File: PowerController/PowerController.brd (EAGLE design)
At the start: 57.1 x 63.5 mm, 97 parts, among them J11 M10X2, Q1 INFINEON_2N7002_DW, Q2 INFINEON_2N7002_DW, Q3 BS250F, Q4 BS250F, Q5 INFINEON_2N7002_DW, Q6 INFINEON_2N7002_DW, Q7 INFINEON_2N7002_DW, U1 MSP430F5521/5/7/9_PN80, U2 LTV-817, U3 SN74LV74, U4 SN74LV08

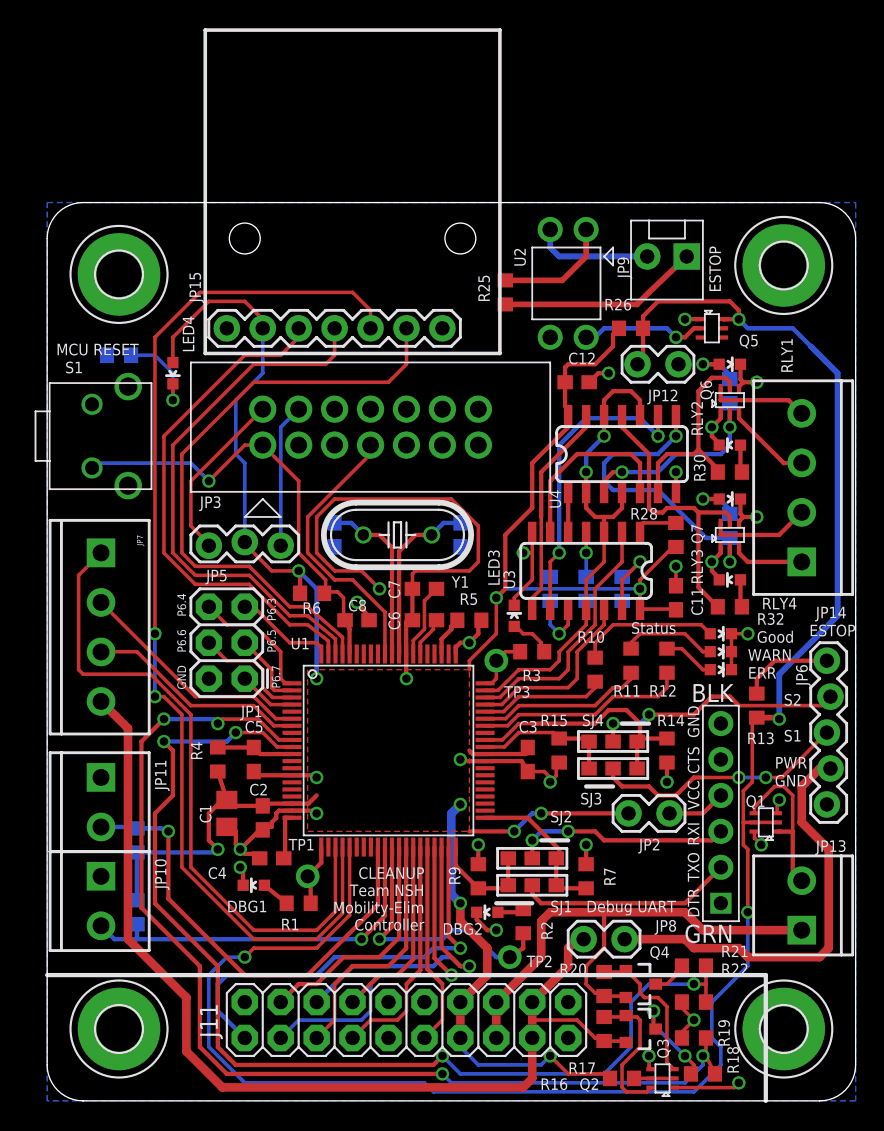
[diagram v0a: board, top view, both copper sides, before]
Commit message: Removed irrelevant circuits for PC2CAN and Power Controller
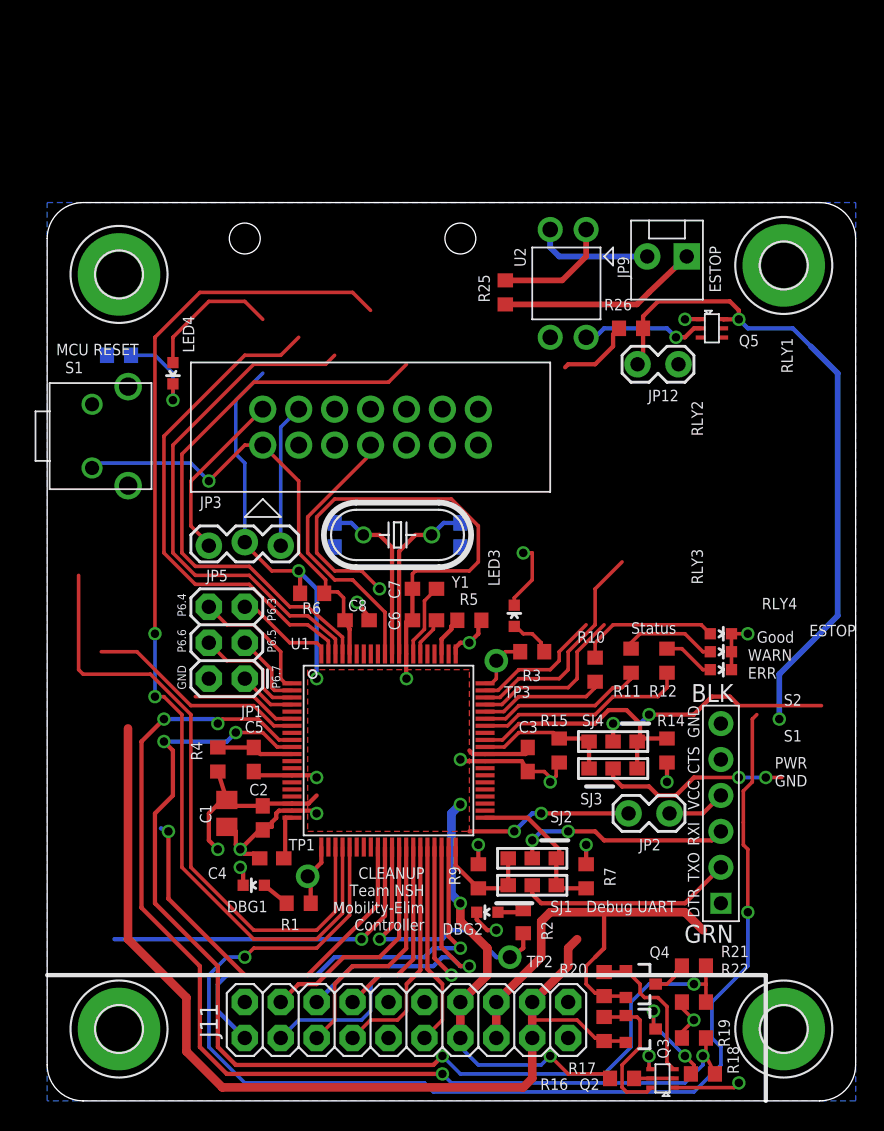
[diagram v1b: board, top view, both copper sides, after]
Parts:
- removed C11, C12: 0.1uF, rcl:C0603
- removed JP10, JP11, JP13: M023.5MM, SparkFun-Connectors:SCREWTERMINAL-3.5MM-2
- removed JP14, JP7: (no value), SparkFun-Connectors:SCREWTERMINAL-3.5MM-4
- removed JP15: (no value), SparkFun-Connectors:1X07
- removed JP6: (no value), SparkFun-Connectors:1X05_LOCK
- removed JP8: M02LOCK, SparkFun-Connectors:1X02_LOCK
- removed LED10, LED11, LED8, LED9: (no value), SparkFun-LED:LED-0603
- removed Q1, Q6, Q7: INFINEON_2N7002_DW, npol-discrete:INFINEON_SOT363
- removed R13, R27, R28, R33, R34: 0, rcl:R0603
- removed R23, R24: 10k, rcl:R0603
- removed R29, R30, R31, R32: 1k, rcl:R0603
- removed U3: SN74LV74, npol-digital:TI_D_R-PDSO-G14_SOIC14
- removed U4: SN74LV08, npol-digital:TI_D_R-PDSO-G14_SOIC14
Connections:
- removed net DRILL_RELAY_1: JP14.4, Q6.6
- removed net DRILL_RELAY_2: JP14.3, Q6.3
- removed net DRILL_RELAY_3: JP14.2, Q7.6
- removed net DRILL_RELAY_4: JP14.1, Q7.3
- removed net ESTOP_RELAY: JP13.2, Q1.1, Q1.4
- removed net N$14: LED9.A, R30.1
- removed net N$20: U3.5, U4.1
- removed net N$22: U3.6, U4.5
- removed net N$23: U3.9, U4.9
- removed net N$25: U3.8, U4.13
- removed net N$26: R27.1, U3.4
- removed net N$27: R28.2, U3.1
- removed net N$28: R33.1, U3.10
- removed net N$29: R34.2, U3.13
- removed net N$33: LED11.A, R32.1
- removed net RC_PWR: JP6.2, JP8.1
- removed net RC_S3: JP6.5, R13.2
- removed net RELAY1_CNTRL: Q6.2, R29.2, U4.3
- removed net RELAY1_LED_A: LED8.A, R29.1
- removed net RELAY2_CNTRL: Q6.5, R30.2, U4.6
- removed net RELAY3_CNTRL: Q7.2, R31.2, U4.8
- removed net RELAY3_LED_A: LED10.A, R31.1
- removed net RELAY4_CNTRL: Q7.5, R32.2, U4.11
- removed net VOC: JP15.7
- net +12V: no longer JP13.1
- net +3V3: no longer C11.1, C12.1, JP15.2, R23.2, R24.2, R27.2, R28.1, R33.2, R34.1, U3.14, U4.14
- net +5V: no longer JP7.4, JP8.2
- net DRILL_EN: no longer U3.11, U3.3, U4.10, U4.12, U4.2, U4.4
- net DRILL_ISENSE_/FAULT: no longer JP15.5
- net DRILL_ISENSE_FAULT_EN: no longer JP15.6
- net DRILL_ISENSE_VIOUT: no longer JP15.3
- net DRILL_ISENSE_VZCR: no longer JP15.4
- net DRILL_S1: no longer U3.2
- net DRILL_S2: no longer U3.12
- net ESTOP_LOCAL: no longer Q1.2, Q1.5, R13.1
- net GND: no longer C11.2, C12.2, JP10.1, JP11.1, JP15.1, JP6.1, LED10.C, LED11.C, LED8.C, LED9.C, Q1.3, Q1.6, Q6.1, Q6.4, Q7.1, Q7.4, U3.7, U4.7
- net LOWER_SWITCH: no longer JP11.2, R24.1
- net RC_S1: no longer JP6.3
- net RC_S2: no longer JP6.4
- net STEPPER_DIR: no longer JP7.2
- net STEPPER_EN: no longer JP7.3
- net STEPPER_STEP: no longer JP7.1
- net UPPER_SWITCH: no longer JP10.2, R23.1
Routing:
- net +3V3: track 162.1 -> 104.0 mm, vias 10 -> 8
- net RC_PWR: track 30.0 -> 0.00 mm
- net DRILL_EN: track 34.1 -> 9.44 mm, vias 2 -> 0
- net RELAY3_CNTRL: track 21.9 -> 0.00 mm, vias 2 -> 0
- net N$23: track 21.6 -> 0.00 mm, vias 2 -> 0
- net RELAY4_CNTRL: track 21.2 -> 0.00 mm
- net GND: track 111.5 -> 92.0 mm, vias 29 -> 20
- net N$25: track 15.2 -> 0.00 mm
- net RELAY2_CNTRL: track 14.8 -> 0.00 mm
- net RELAY1_CNTRL: track 14.8 -> 0.00 mm, vias 2 -> 0
- net N$22: track 13.1 -> 0.00 mm
- net ESTOP_RELAY: track 11.4 -> 0.00 mm
- net STEPPER_DIR: track 16.9 -> 7.48 mm
- net DRILL_RELAY_3: track 7.18 -> 0.00 mm
- net +12V: track 38.2 -> 31.2 mm
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
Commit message: Power Controller ready for fab
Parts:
- removed JP12: M02LOCK, SparkFun-Connectors:1X02_LOCK
- removed JP9: M02POLAR_LOCK, SparkFun-Connectors:MOLEX-1X2_LOCK
- removed U2: LTV-817, npol-digital:LITEON_DIL04_.3
- added JP6: (no value), SparkFun-Connectors:1X03_LOCK
- added JP7: M02POLAR_LOCK, SparkFun-Connectors:MOLEX-1X2_LOCK
- added LED10, LED8, LED9: (no value), SparkFun-LED:LED-0603
- added Q1: INFINEON_2N7002_DW, npol-discrete:INFINEON_SOT363
- added R13, R23: 10k, rcl:R0603
- added R24: 470, rcl:R0603
- added R27: 330, rcl:R0603
- added XB1: XBEE, microbuilder:XBEE
- H3: value MOUNT-PAD-ROUND3.2 -> MOUNT-HOLE3.2; device holes:3,2-PAD -> holes:3,2
- JP1: device SparkFun-Connectors:2X3 -> SparkFun-Connectors:1X05
- JP2: value M02LOCK -> (none); device SparkFun-Connectors:1X02_LOCK -> SparkFun-Connectors:2X3
- JP3: value ONSHORE_OST302-S141 -> M02LOCK; device npol-connectors:ONSHORE_OST302-S141 -> SparkFun-Connectors:1X02_LOCK
- JP4: value FTDI_DEVICE -> ONSHORE_OST302-S141; device SparkFun-Connectors:FTDI_DEVICE_SIDE -> npol-connectors:ONSHORE_OST302-S141
- JP5: value (none) -> FTDI_DEVICE; device SparkFun-Connectors:1X03_LOCK -> SparkFun-Connectors:FTDI_DEVICE_SIDE
- Q2: value INFINEON_2N7002_DW -> BS250F; device npol-discrete:INFINEON_SOT363 -> SparkFun-DiscreteSemi:SOT23-3
- Q4: value BS250F -> INFINEON_2N7002_DW; device SparkFun-DiscreteSemi:SOT23-3 -> npol-discrete:INFINEON_SOT363
- R17, R20: value 10k -> 100k
- R19, R21: value 100k -> 10k
- R25: value 620 -> 330
- R26: value 10k -> 470
- moved R22 50.4 mm to (12.7, 45.1), turned to 180 degrees
- moved JP5 44.7 mm to (55.2, 17.1), turned to 90 degrees
- moved JP4 42.6 mm to (5.08, 22.2), turned to 270 degrees
- moved Q4 42.4 mm to (24.8, 47.0), turned to 180 degrees
- moved JP1 37.2 mm to (49.5, 19.1), turned to 180 degrees
- moved JP3 31.7 mm to (33.7, 17.8)
- moved Q5 31.0 mm to (17.1, 46.4)
- moved JP2 28.9 mm to (14.0, 29.8), turned to 90 degrees
- moved R8 26.0 mm to (30.5, 47.0), flipped to the top, turned to 0 degrees
- moved R25 25.8 mm to (9.53, 45.1), turned to 90 degrees
- moved R15 23.6 mm to (40.6, 1.59), turned to 180 degrees
- moved LED4 21.7 mm to (30.5, 48.9), turned to 90 degrees
- moved R26 17.6 mm to (24.1, 50.8), turned to 270 degrees
- moved R14 12.1 mm to (35.6, 33.7), turned to 270 degrees
- moved R3 11.3 mm to (31.1, 42.5), turned to 270 degrees
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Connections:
- removed net DRILL_EN: U1.59
- removed net DRILL_ISENSE_/FAULT: U1.24
- removed net DRILL_ISENSE_FAULT_EN: U1.77
- removed net DRILL_ISENSE_VIOUT: U1.79
- removed net DRILL_ISENSE_VZCR: U1.78
- removed net DRILL_S1: U1.58
- removed net DRILL_S2: U1.57
- removed net ESTOP+: JP9.1, R25.2
- removed net ESTOP-: JP9.2, U2.2
- removed net ESTOP_LOCAL: JP12.1, Q5.6, R26.2, U1.25
- removed net ESTOP_LOCAL_INV: Q5.2, U2.4
- removed net LOWER_SWITCH: U1.29
- removed net RC_RXD: R14.2, SJ3.3, SJ4.1, U1.52
- removed net RC_S1: SJ3.2
- removed net RC_S2: SJ4.2
- removed net RC_TXD: R15.2, SJ3.1, SJ4.3, U1.51
- removed net STEPPER_DIR: U1.6
- removed net STEPPER_EN: U1.7
- removed net STEPPER_STEP: U1.23
- removed net UPPER_SWITCH: U1.30
- new net ESTOP_INV: LED8.C, Q4.5, Q4.6, R23.2, U1.22
- new net ESTOP_OUT: JP7.1, Q4.2, Q5.6, R25.2
- new net ESTOP_PULLDOWN: Q5.2, Q5.5, R22.1, U1.23
- new net N$14: LED10.C, R27.1
- new net N$15: LED8.A, R24.2
- new net N$16: Q4.3, R26.2
- new net N$17: LED9.C, R26.1
- new net NU_P3.7: JP1.5, U1.44
- new net NU_P4.0: JP1.4, U1.45
- new net NU_P4.1: JP1.3, U1.46
- new net NU_P4.2: JP1.2, U1.47
- new net NU_P4.3: JP1.1, U1.48
- new net XBEE_DIN: SJ3.2, XB1.3
- new net XBEE_DOUT: SJ4.2, XB1.2
- new net XBEE_RXD: R13.2, SJ3.3, SJ4.1, U1.52
- new net XBEE_TXD: R14.2, SJ3.1, SJ4.3, U1.51
- net +12V: now also Q3.2, R19.2, R25.1; no longer Q4.2, R20.2
- net +3V3: now also JP3.1, JP6.2, LED10.A, LED9.A, R15.2, R23.1, R24.1, XB1.1; no longer JP2.1, JP5.2, R16.2, R26.1
- net +5V: now also Q2.2, R16.2; no longer Q3.2, R17.2
- net 12VSENSE: now also R20.1, R21.2; no longer R21.1, R22.2
- net 5VSENSE: now also R17.1, R18.2; no longer R18.1, R19.2
- net GND: now also JP2.2, JP4.9, JP5.P$6, JP7.2, Q1.1, Q1.4, Q4.1, Q4.4, Q5.4, R13.1, R18.1, R21.1, R22.2, XB1.10; no longer H3.B3,2, JP1.2, JP12.2, JP3.9, JP4.P$6, Q2.1, Q2.4, R15.1, R19.1, R22.1, U2.3
- net N$1: now also JP3.2, JP5.P$4; no longer JP2.2, JP4.P$4
- net N$10: now also Q1.6, Q2.1, R16.1; no longer Q2.6, Q3.1, R17.1
- net N$11: now also Q3.3, R20.2; no longer Q4.3, R21.2
- net N$12: now also Q1.2, Q1.5, R15.1; no longer Q2.2, Q2.5, R16.1
- net N$13: now also Q5.3, R27.2; no longer R25.1, U2.1
- net N$9: now also Q2.3, R17.2; no longer Q3.3, R18.2
- net NU_P6.3: now also JP2.5; no longer JP1.5
- net NU_P6.4: now also JP2.6; no longer JP1.6
- net NU_P6.5: now also JP2.3; no longer JP1.3
- net NU_P6.6: now also JP2.4; no longer JP1.4
- net NU_P6.7: now also JP2.1; no longer JP1.1
- net RXI: now also JP5.P$3; no longer JP4.P$3
- net SBWTCK: now also JP4.7; no longer JP3.7
- net SBWTDIO: now also JP4.1; no longer JP3.1
- net TXO: now also JP5.P$2; no longer JP4.P$2
- net VCC_TARGET: now also JP4.4, JP6.1; no longer JP3.4, JP5.1
- net VCC_TOOL: now also JP4.2, JP6.3; no longer JP3.2, JP5.3
- net VTAP_EN: now also Q1.3, Q3.1, R19.1; no longer Q2.3, Q4.1, R20.1
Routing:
- net ESTOP_LOCAL: track 134.1 -> 0.00 mm, vias 4 -> 0
- net DRILL_ISENSE_/FAULT: track 74.6 -> 0.00 mm, vias 2 -> 0
- net ESTOP_INV: track 0.00 -> 70.8 mm, vias 0 -> 2
- net +12V: track 31.2 -> 91.7 mm
- net +5V: track 69.3 -> 10.6 mm
- net ESTOP_PULLDOWN: track 0.00 -> 58.1 mm, vias 0 -> 2
- net STEPPER_STEP: track 43.9 -> 0.00 mm
- net DRILL_ISENSE_FAULT_EN: track 40.4 -> 0.00 mm
- net DRILL_ISENSE_VZCR: track 36.7 -> 0.00 mm
- net DRILL_ISENSE_VIOUT: track 35.7 -> 0.00 mm
- net ESTOP_OUT: track 0.00 -> 29.5 mm
- net XBEE_DIN: track 0.00 -> 28.6 mm
- net LOWER_SWITCH: track 28.5 -> 0.00 mm, vias 1 -> 0
- net SBWTCK: track 19.6 -> 47.0 mm, vias 0 -> 2
- net UPPER_SWITCH: track 24.7 -> 0.00 mm, vias 1 -> 0
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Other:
- board size 57.1 x 63.5 mm -> 57.1 x 54.6 mm
- board text added: "CLEANUP Team NSH Power Controller"
- board text added: "ES+"
- board text added: "ES-"
- board text added: "P3.7"
- board text added: "P4.0"
- board text added: "P4.1"
- board text added: "P4.2"
- board text added: "P4.3"
- board text added: "PULL"
- board text added: "Plastic Screw"
- board text removed: "CLEANUP Team NSH Mobility-Elim Controller"
- board text removed: "PWR"
- board text removed: "RLY1"
- board text removed: "RLY2"
- board text removed: "RLY3"
- board text removed: "RLY4"
- board text removed: "S1"
- board text removed: "S2"

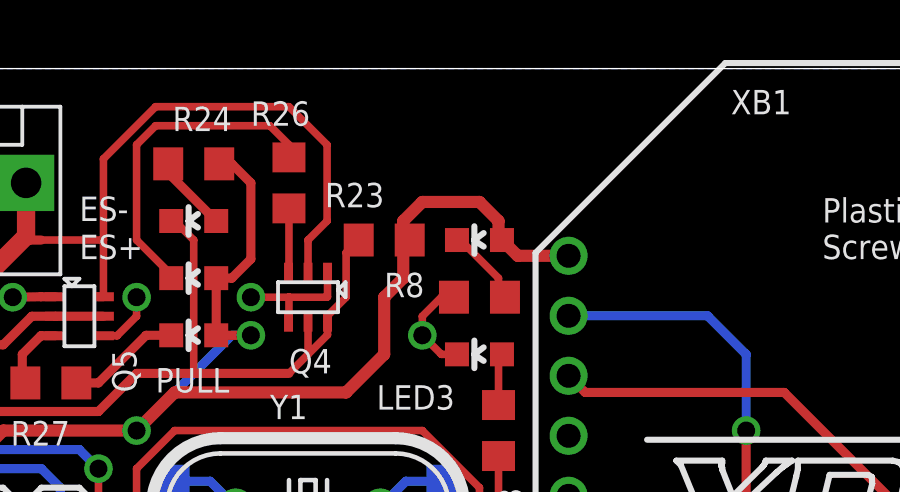
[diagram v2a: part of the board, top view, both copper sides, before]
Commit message: Power Controller, Elim-Mobility Controller, and PC2CAN sent to FAB
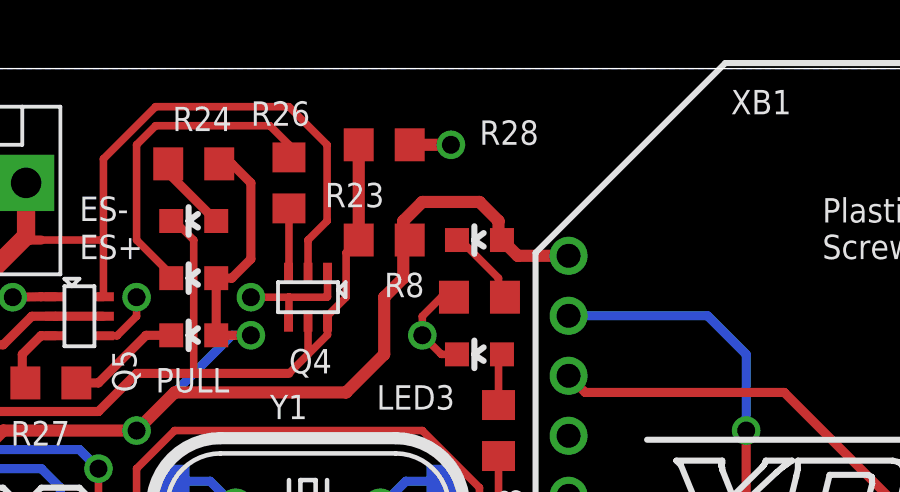
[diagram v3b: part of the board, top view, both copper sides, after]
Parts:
- added R28: 10M, rcl:R0603
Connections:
- net ESTOP_INV: now also R28.1
- net GND: now also R28.2
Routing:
- net ESTOP_INV: track 70.8 -> 74.0 mm
- net GND: track 96.4 -> 97.8 mm, vias 24 -> 25
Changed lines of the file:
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@@
 <polygon width="0.4064" layer="42">
 <vertex x="57.15" y="54.61"/>
-<vertex x="27.305" y="54.61"/>
-<vertex x="27.305" y="49.53"/>
+<vertex x="30.48" y="54.61"/>
+<vertex x="30.48" y="49.53"/>
 <vertex x="57.15" y="49.53"/>
 </polygon>
@@
 <attribute name="NAME" x="13.97" y="46.99" size="0.8128" layer="25" rot="R180"/>
 </element>
+<element name="R28" library="rcl" package="R0603" value="10M" x="27.305" y="52.07" smashed="yes">
+<attribute name="NAME" x="30.48" y="52.07" size="0.8128" layer="25"/>
+</element>
 </elements>
 <signals>
@@
 <wire x1="24.13" y1="46.205" x2="24.115" y2="46.19" width="0.254" layer="1"/>
 <wire x1="22.86" y1="46.99" x2="24.13" y2="46.99" width="0.254" layer="1"/>
+<contactref element="R28" pad="2"/>
+<via x="29.5275" y="52.07" extent="1-16" drill="0.6"/>
+<wire x1="28.155" y1="52.07" x2="29.5275" y2="52.07" width="0.4064" layer="1"/>
 </signal>
 <signal name="CAN_STBY">
@@
 <wire x1="26.035" y1="46.99" x2="26.035" y2="48.475" width="0.254" layer="1"/>
 <wire x1="26.035" y1="48.475" x2="26.455" y2="48.895" width="0.254" layer="1"/>
+<contactref element="R28" pad="1"/>
+<wire x1="26.455" y1="52.07" x2="26.455" y2="48.895" width="0.4064" layer="1"/>
 </signal>
 <signal name="N$15">
